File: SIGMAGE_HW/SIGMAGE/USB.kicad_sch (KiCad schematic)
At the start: 27 parts, among them J1 UJ31CHG2SMTTR, U13 ESDR0502NMUTBG, U9 FT2232HLTRAY

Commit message: more USB stuff
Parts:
- added C46: 100n, Capacitor_SMD:C_0603_1608Metric, symbol Device:C
- added C47, C48: 18p, Capacitor_SMD:C_0603_1608Metric, symbol Device:C
- added CR1: 7M12MAAJT, SIGMAGE:7M12MAAJT, symbol SIGMAGE:7M12MAAJT
- added J3: TSW10607GS, SIGMAGE:TSW10607GS, symbol SIGMAGE:TSW10607GS
- added R22, R26, R27: 10k, Resistor_SMD:R_0603_1608Metric, symbol Device:R
- added R28: 2200, Resistor_SMD:R_0603_1608Metric, symbol Device:R
- added R29, R30, R31: 4700, Resistor_SMD:R_0603_1608Metric, symbol Device:R
- added R43: 12k, Resistor_SMD:R_0603_1608Metric, symbol Device:R
- added R44, R45, R46, R47: 0, Resistor_SMD:R_0603_1608Metric, symbol Device:R
- added U14: 93LC56-I/SN, SIGMAGE:93LC56ISN, symbol SIGMAGE:93LC56ISN
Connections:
- net DVCC_3V3: now also C46.1, J3.1, R22.2, R26.2, R27.2, R29.2, R30.2, R31.2, U14.6 (ORG), U14.8 (VCC)
- net GND: now also C46.2, C47.2, C48.2, CR1.2, CR1.4, J3.6, R28.1, U14.5 (VSS)
- net at U9.16 (ADBUS0): now also R44.1
- net at U9.17 (ADBUS1): now also R45.1
- net at U9.18 (ADBUS2): now also R46.1
- net at U9.19 (ADBUS3): now also R47.1
- net at U9.2 (OSCI): now also C47.1, CR1.1
- net at U9.3 (OSCO): now also C48.1, CR1.3
- net FPGA_UART_TXD: now reaches U9.38 (BDBUS0)
- net FPGA_UART_RXD: now reaches U9.39 (BDBUS1)
- net at U9.61 (EEDATA): now also R43.2, U14.3 (DI)
- net at U9.62 (EECLK): now also R26.1, U14.2 (CLK)
- net at U9.63 (EECS): now also R22.1, U14.1 (CS)
- new net: R27.1, R43.1, U14.4 (DO)
- new net FPGA_JTAG_TCK: J3.5, R28.2, R44.2
- new net FPGA_JTAG_TDI: J3.4, R31.1, R45.2
- new net FPGA_JTAG_TDO: J3.3, R30.1, R46.2
- new net FPGA_JTAG_TMS: J3.2, R29.1, R47.2
- no-connect marks 37 -> 39
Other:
- moved on the sheet: C10, C11, C33, C34, C35, C36, C37, C38, C39, C40, C41, C42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

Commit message: some FPGA stuff
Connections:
- net DVCC_3V3: no longer J3.1, R29.2, R30.2, R31.2
- new net VCC_IO8: J3.1, R29.2, R30.2, R31.2
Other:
- moved on the sheet: C37, C38, C39, C40, C41, C42, C43, C44, C45

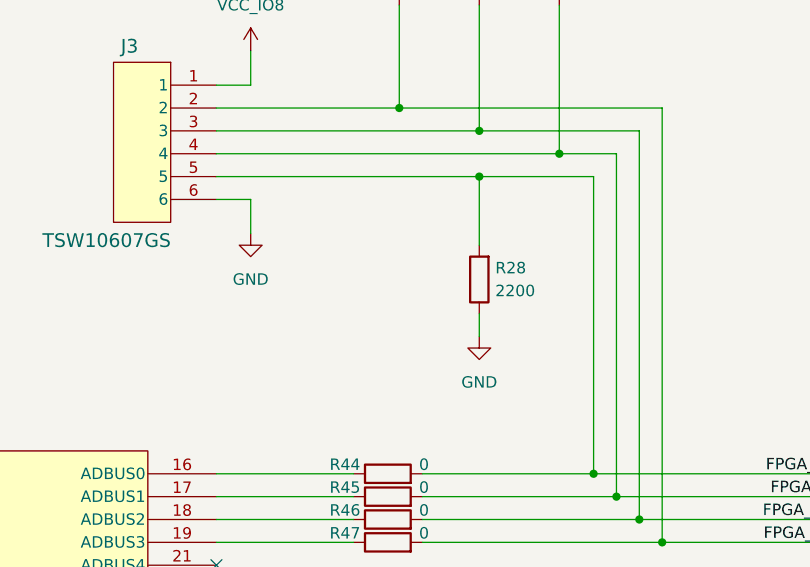
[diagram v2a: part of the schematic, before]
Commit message: added SPI flash
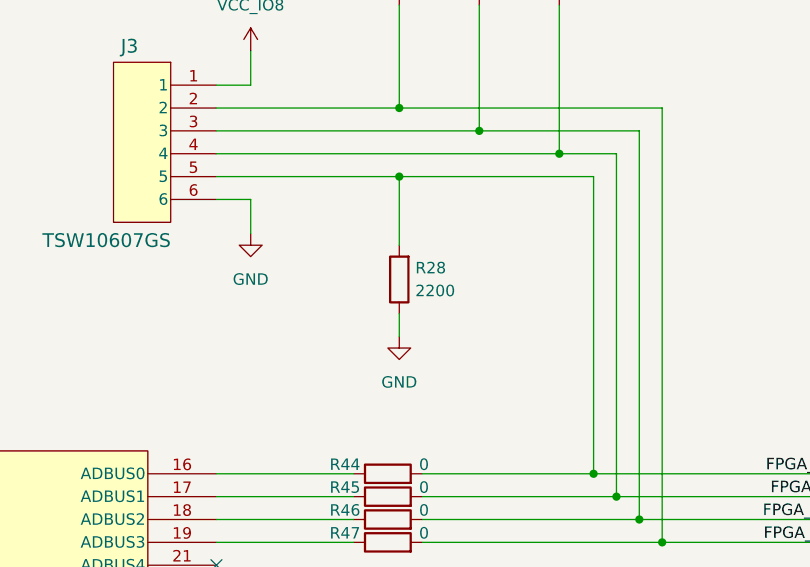
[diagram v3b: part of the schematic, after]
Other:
- moved on the sheet: R28

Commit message: some changes
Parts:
- FB6, FB7: value 600 @ 100 MHz -> 500 @ 100 MHz
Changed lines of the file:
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@@
 			)
 		)
-		(property "Value" "600 @ 100 MHz"
+		(property "Value" "500 @ 100 MHz"
 			(at 63.5 141.478 90)
 			(show_name no)
@@
 			)
 		)
-		(property "Value" "600 @ 100 MHz"
+		(property "Value" "500 @ 100 MHz"
 			(at 63.5 121.158 90)
 			(show_name no)

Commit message: changes
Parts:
- removed R44, R45, R46, R47: 0, Resistor_SMD:R_0603_1608Metric, symbol Device:R
- added J6: TSW10607GS, SIGMAGE:TSW10607GS, symbol SIGMAGE:TSW10607GS
- added R59, R61, R62: 4700, Resistor_SMD:R_0603_1608Metric, symbol Device:R
- added R60: 2200, Resistor_SMD:R_0603_1608Metric, symbol Device:R
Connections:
- net VCC_IO8 is gone; now on net DVCC_3V3: J3.1, R29.2, R30.2, R31.2
- net DVCC_3V3: now also J6.1, R59.2, R61.2, R62.2
- net FPGA_JTAG_TCK: now also U9.16 (ADBUS0)
- net FPGA_JTAG_TDI: now also R29.1, U9.17 (ADBUS1); no longer R31.1
- net FPGA_JTAG_TDO: now also U9.18 (ADBUS2)
- net FPGA_JTAG_TMS: now also R31.1, U9.19 (ADBUS3); no longer R29.1
- net GND: now also J6.6, R60.1
- net MCU_JTAG_TDO: now reaches U9.40 (BDBUS2)
- net MCU_JTAG_TDO: now also J6.3, R61.1
- net MCU_JTAG_TMS: now reaches U9.41 (BDBUS3)
- net MCU_JTAG_TMS: now also J6.2, R62.1
- net FPGA_UART_RXD renamed MCU_JTAG_TDI
- net MCU_JTAG_TDI: now also J6.4, R59.1
- net FPGA_UART_TXD renamed MCU_JTAG_TCK
- net MCU_JTAG_TCK: now also J6.5, R60.2
- no-connect marks 39 -> 37
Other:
- moved on the sheet: C10, C11, C33, C34, C35, C36, C37, C38, C39, C40, C41, C42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

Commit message: major changes
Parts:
- R12: value 100 -> 150
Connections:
- net DVCC_3V3: no longer U9.49 (VREGOUT)
- net VCCFT_1V8 renamed DVCCFT_1V8
- net DVCCFT_1V8: now also U9.49 (VREGOUT)

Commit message: almost done
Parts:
- C10, C11: value 2u2 -> 2.2u
- FB6, FB7: value 500 @ 100 MHz -> 600 @ 100 MHz
- R12: value 150 -> 1500
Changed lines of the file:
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@@
 			)
 		)
-		(property "Value" "150"
+		(property "Value" "1500"
 			(at 375.158 148.59 0)
 			(show_name no)
@@
 			)
 		)
-		(property "Value" "500 @ 100 MHz"
+		(property "Value" "600 @ 100 MHz"
 			(at 55.88 141.478 90)
 			(show_name no)
@@
 			)
 		)
-		(property "Value" "2u2"
+		(property "Value" "2.2u"
 			(at 359.918 148.59 0)
 			(show_name no)
@@
 			)
 		)
-		(property "Value" "500 @ 100 MHz"
+		(property "Value" "600 @ 100 MHz"
 			(at 55.88 121.158 90)
 			(show_name no)
@@
 			)
 		)
-		(property "Value" "2u2"
+		(property "Value" "2.2u"
 			(at 325.628 148.59 0)
 			(show_name no)

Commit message: finished schematic
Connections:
- net USB_DN: no longer J1.A7 (DN1), J1.B7 (DN2), U13.3 (NC), U13.4 (D-)
- net USB_DP: no longer J1.A6 (DP1), J1.B6 (DP2), U13.2 (NC), U13.5 (D+)
- net FPGA_JTAG_TCK renamed 0_FPGA_JTAG_TCK
- net FPGA_JTAG_TDI renamed 0_FPGA_JTAG_TDI
- net FPGA_JTAG_TDO renamed 0_FPGA_JTAG_TDO
- net FPGA_JTAG_TMS renamed 0_FPGA_JTAG_TMS
- net MCU_JTAG_TCK renamed 0_MCU_JTAG_TCK
- net MCU_JTAG_TDI renamed 0_MCU_JTAG_TDI
- net MCU_JTAG_TDO renamed 0_MCU_JTAG_TDO
- net MCU_JTAG_TMS renamed 0_MCU_JTAG_TMS
- new net 0_USB_DN: J1.A7 (DN1), J1.B7 (DN2), U13.3 (NC), U13.4 (D-)
- new net 0_USB_DP: J1.A6 (DP1), J1.B6 (DP2), U13.2 (NC), U13.5 (D+)
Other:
- moved on the sheet: R10, R11
